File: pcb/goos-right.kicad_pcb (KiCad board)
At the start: 2 copper layers, 142.9 x 112.6 mm, 22 parts

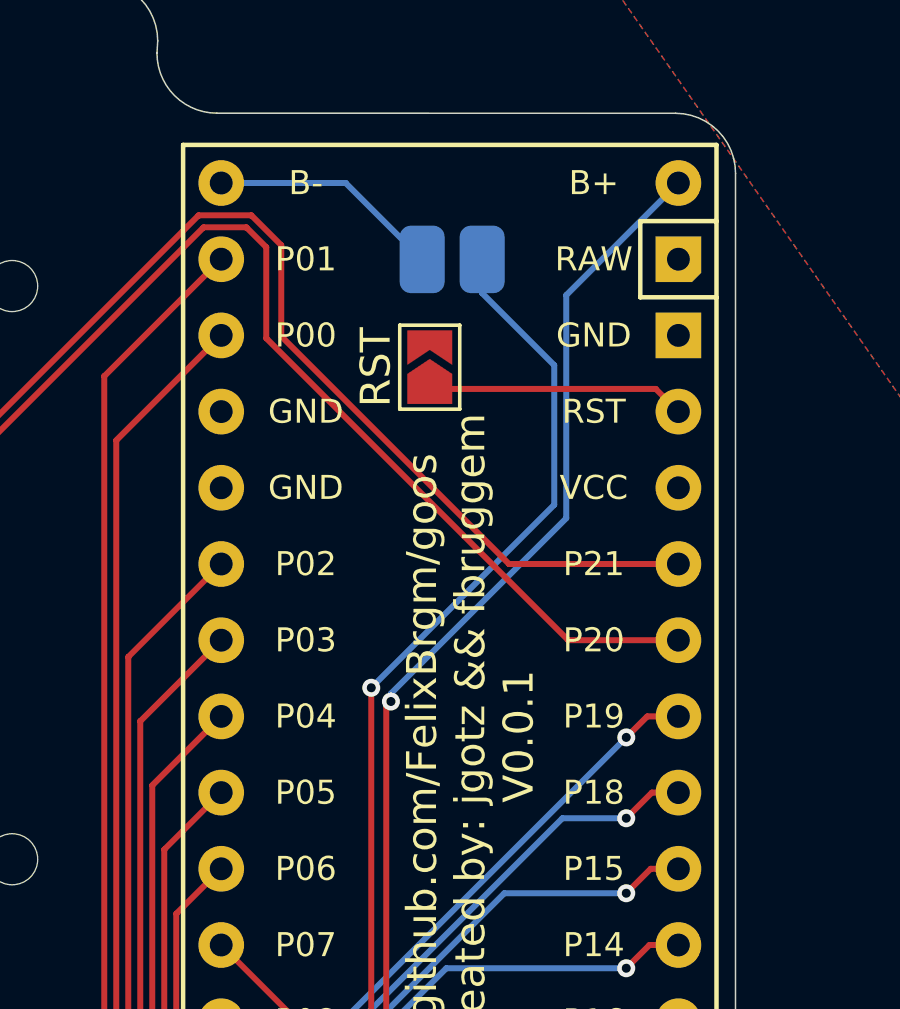
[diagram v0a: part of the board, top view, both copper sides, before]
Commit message: fix: move pads further apart
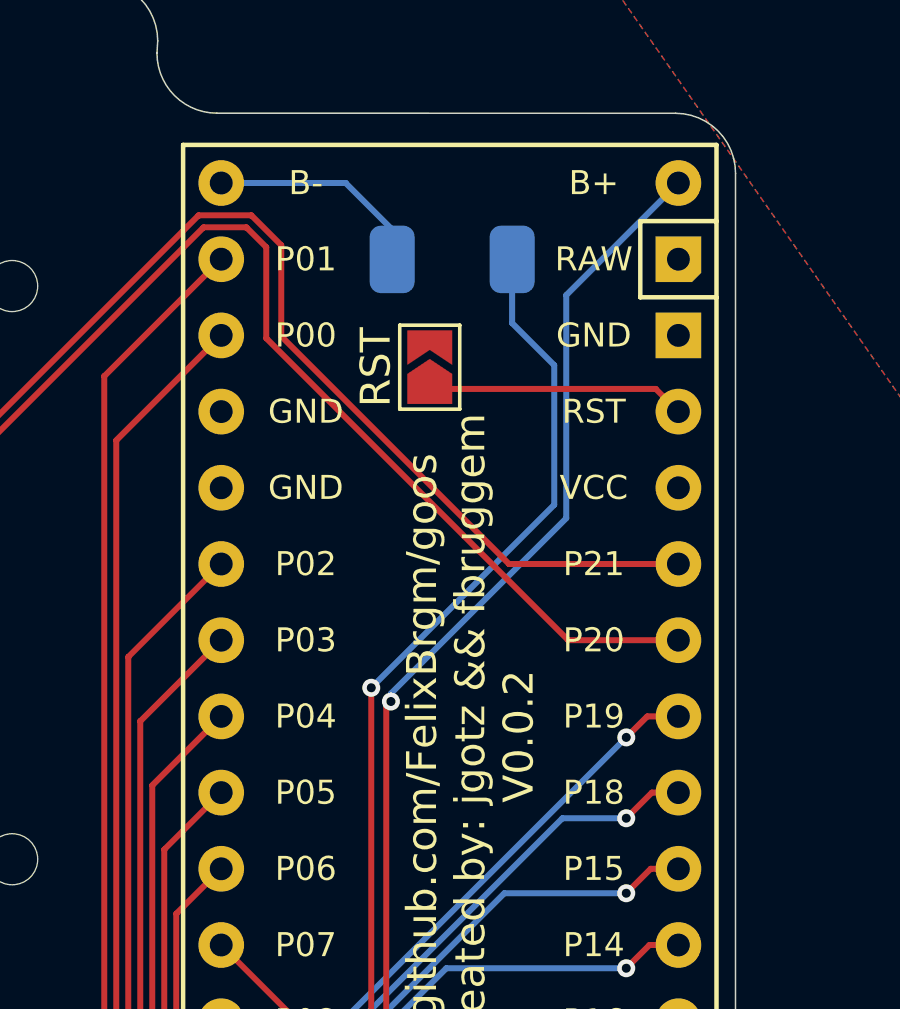
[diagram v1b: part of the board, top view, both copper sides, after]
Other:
- board text added: "github.com/FelixBrgm/goos Created by: jgotz && fbruggem V0.0.2"
- board text removed: "github.com/FelixBrgm/goos Created by: jgotz && fbruggem V0.0.1"
